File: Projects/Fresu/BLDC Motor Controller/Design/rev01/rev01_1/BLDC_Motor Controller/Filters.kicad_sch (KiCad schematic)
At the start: 0 parts

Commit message: UPDATE 9
COMPLETED FILTERS SCHEMATIC
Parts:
- added C44, C50, C52, C54: 100n, symbol Device:C
- added C48, C49, C51, C53: 4n7, symbol Device:C
- added J8: Conn_01x06, symbol Connector_Generic:Conn_01x06
- added R38, R44, R46: 2k2, symbol Device:R
- added R43, R45, R47, R48: 10k, symbol Device:R
- added R49: 0R, symbol Device:R
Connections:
- new net +3V3: C44.1, C50.1, C52.1, C54.1, R38.1, R44.1, R46.1, R48.1
- new net +5V: J8.1 (Pin_1)
- new net GND: C44.2, C48.2, C49.2, C50.2, C51.2, C52.2, C53.2, C54.2, J8.6 (Pin_6)
- new net HALL_1_IN: C48.1, J8.3 (Pin_3), R38.2, R43.1
- new net HALL_1_OUT: R43.2
- new net HALL_2_IN: C49.1, J8.4 (Pin_4), R44.2, R45.1
- new net HALL_2_OUT: R45.2
- new net HALL_3_IN: C51.1, J8.5 (Pin_5), R46.2, R47.1
- new net HALL_3_OUT: R47.2
- new net TEMP_IN: C53.1, J8.2 (Pin_2), R48.2, R49.1
- new net TEMP_MOTOR: R49.2
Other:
- note added: "HALL ENCODER TO MCU =>"
- note added: "HALL_1 FILTER"
- note added: "HALL_2 FILTER"
- note added: "HALL_3 FILTER"
- note added: "OUTPUT"
- note added: "TEMP_MOTOR FILTER"

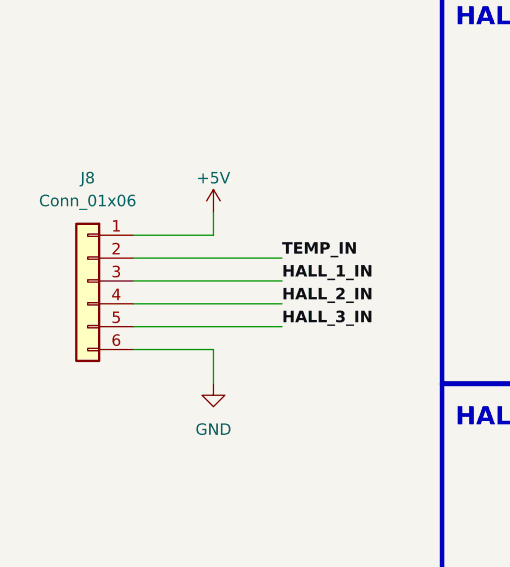
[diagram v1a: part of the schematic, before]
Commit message: Update 13
Added:
1) USB Schematic
2) footprints to all parts
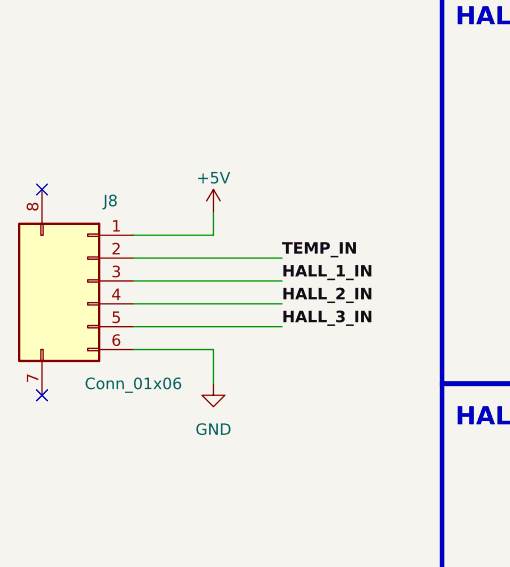
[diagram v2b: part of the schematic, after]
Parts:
- C44, C48, C49, C50, C51, C52, C53, C54: footprint (none) -> Capacitor_SMD:C_0603_1608Metric
- J8: footprint (none) -> DF_ESC_Footprint_Library:CONN-SMD_S6B-XH-SM4-TB-LF-SN
- R38, R43, R44, R45, R46, R47, R48, R49: footprint (none) -> Resistor_SMD:R_0603_1608Metric_Pad0.98x0.95mm_HandSolder
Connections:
- no-connect marks 0 -> 2
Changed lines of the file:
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@@
   (junction (at 93.98 41.91) (diameter 0) (color 0 0 0 0)
   )
+  (no_connect (at 22.86 104.14))
+  (no_connect (at 22.86 81.28))
   (polyline (pts (xy 128.27 58.42) (xy 67.31 58.42))
     (stroke (width 0.5) (type default))
@@
       (effects (font (size 1.27 1.27)) (justify left))
     )
-    (property "Footprint" "" (at 92.202 76.2 90)
+    (property "Footprint" "Resistor_SMD:R_0603_1608Metric_Pad0.98x0.95mm_HandSolder" (at 92.202 76.2 90)
       (effects (font (size 1.27 1.27)) hide)
     )
@@
       (effects (font (size 1.27 1.27)) (justify left))
     )
-    (property "Footprint" "" (at 110.1852 121.92 0)
+    (property "Footprint" "Capacitor_SMD:C_0603_1608Metric" (at 110.1852 121.92 0)
       (effects (font (size 1.27 1.27)) hide)
     )
@@
       (effects (font (size 1.27 1.27)) (justify left))
     )
-    (property "Footprint" "" (at 110.1852 33.02 0)
+    (property "Footprint" "Capacitor_SMD:C_0603_1608Metric" (at 110.1852 33.02 0)
       (effects (font (size 1.27 1.27)) hide)
     )
@@
       (effects (font (size 1.27 1.27)) (justify left))
     )
-    (property "Footprint" "" (at 110.1852 77.47 0)
+    (property "Footprint" "Capacitor_SMD:C_0603_1608Metric" (at 110.1852 77.47 0)
       (effects (font (size 1.27 1.27)) hide)
     )
@@
       (effects (font (size 1.27 1.27)) (justify left))
     )
-    (property "Footprint" "" (at 94.9452 52.07 0)
+    (property "Footprint" "Capacitor_SMD:C_0603_1608Metric" (at 94.9452 52.07 0)
       (effects (font (size 1.27 1.27)) hide)
     )
@@
       (effects (font (size 1.27 1.27)))
     )
-    (property "Footprint" "" (at 102.87 177.038 90)
+    (property "Footprint" "Resistor_SMD:R_0603_1608Metric_Pad0.98x0.95mm_HandSolder" (at 102.87 177.038 90)
       (effects (font (size 1.27 1.27)) hide)
     )
@@
       (effects (font (size 1.27 1.27)))
     )
-    (property "Footprint" "" (at 102.87 88.138 90)
+    (property "Footprint" "Resistor_SMD:R_0603_1608Metric_Pad0.98x0.95mm_HandSolder" (at 102.87 88.138 90)
       (effects (font (size 1.27 1.27)) hide)
     )
@@
       (effects (font (size 1.27 1.27)) (justify left))
     )
-    (property "Footprint" "" (at 92.202 120.65 90)
+    (property "Footprint" "Resistor_SMD:R_0603_1608Metric_Pad0.98x0.95mm_HandSolder" (at 92.202 120.65 90)
       (effects (font (size 1.27 1.27)) hide)
     )
@@
       (effects (font (size 1.27 1.27)) (justify left))
     )
-    (property "Footprint" "" (at 110.1852 166.37 0)
+    (property "Footprint" "Capacitor_SMD:C_0603_1608Metric" (at 110.1852 166.37 0)
       (effects (font (size 1.27 1.27)) hide)
     )
@@
   (symbol (lib_id "Connector_Generic:Conn_01x06") (at 27.94 91.44 0) (mirror y) (unit 1)
     (in_bom yes) (on_board yes) (dnp no) (fields_autoplaced)
-    (property "Reference" "J8" (at 27.94 80.01 0)
-      (effects (font (size 1.27 1.27)))
-    )
-    (property "Value" "Conn_01x06" (at 27.94 82.55 0)
-      (effects (font (size 1.27 1.27)))
-    )
-    (property "Footprint" "" (at 27.94 91.44 0)
+    (property "Reference" "J8" (at 30.48 82.55 0)
+      (effects (font (size 1.27 1.27)))
+    )
+    (property "Value" "Conn_01x06" (at 33.02 102.87 0)
+      (effects (font (size 1.27 1.27)))
+    )
+    (property "Footprint" "DF_ESC_Footprint_Library:CONN-SMD_S6B-XH-SM4-TB-LF-SN" (at 27.94 91.44 0)
       (effects (font (size 1.27 1.27)) hide)
     )
@@
     (pin "1")
     (pin "2")
+    (pin "8")
+    (pin "7")
     (instances
       (project "BLDC_Motor Controller"
@@
       (effects (font (size 1.27 1.27)) (justify left))
     )
-    (property "Footprint" "" (at 92.202 165.1 90)
+    (property "Footprint" "Resistor_SMD:R_0603_1608Metric_Pad0.98x0.95mm_HandSolder" (at 92.202 165.1 90)
       (effects (font (size 1.27 1.27)) hide)
     )
@@
       (effects (font (size 1.27 1.27)) (justify left))
     )
-    (property "Footprint" "" (at 94.9452 140.97 0)
+    (property "Footprint" "Capacitor_SMD:C_0603_1608Metric" (at 94.9452 140.97 0)
       (effects (font (size 1.27 1.27)) hide)
     )
@@
       (effects (font (size 1.27 1.27)) (justify left))
     )
-    (property "Footprint" "" (at 92.202 31.75 90)
+    (property "Footprint" "Resistor_SMD:R_0603_1608Metric_Pad0.98x0.95mm_HandSolder" (at 92.202 31.75 90)
       (effects (font (size 1.27 1.27)) hide)
     )
@@
       (effects (font (size 1.27 1.27)))
     )
-    (property "Footprint" "" (at 102.87 132.588 90)
+    (property "Footprint" "Resistor_SMD:R_0603_1608Metric_Pad0.98x0.95mm_HandSolder" (at 102.87 132.588 90)
       (effects (font (size 1.27 1.27)) hide)
     )
@@
       (effects (font (size 1.27 1.27)) (justify left))
     )
-    (property "Footprint" "" (at 94.9452 185.42 0)
+    (property "Footprint" "Capacitor_SMD:C_0603_1608Metric" (at 94.9452 185.42 0)
       (effects (font (size 1.27 1.27)) hide)
     )
@@
       (effects (font (size 1.27 1.27)) (justify left))
     )
-    (property "Footprint" "" (at 94.9452 96.52 0)
+    (property "Footprint" "Capacitor_SMD:C_0603_1608Metric" (at 94.9452 96.52 0)
       (effects (font (size 1.27 1.27)) hide)
     )
@@
       (effects (font (size 1.27 1.27)))
     )
-    (property "Footprint" "" (at 102.87 43.688 90)
-      (effects (font (size 1.27 1.27)) hide)
-    )
+    (property "Footprint" "Resistor_SMD:R_0603_1608Metric_Pad0.98x0.95mm_HandSolder" (at 102.87 43.688 90)
+      (effects (font (size 1.27 1.27)) hide)
+    )

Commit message: Update 15
Fixing some schematic errors

initial layout of larger component complete
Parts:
- removed J8: Conn_01x06, DF_ESC_Footprint_Library:CONN-SMD_S6B-XH-SM4-TB-LF-SN, symbol Connector_Generic:Conn_01x06
- added J7: Conn_01x06, DF_ESC_Footprint_Library:CONN-SMD_S6B-XH-SM4-TB-LF-SN, symbol Connector_Generic:Conn_01x06
- renumbered C48 to C47, C49 to C48, C51 to C49, C53 to C50, C44 to C51, C50 to C52, C52 to C53, R38 to R43, R46 to R45, R48 to R46, R43 to R47, R45 to R48, R47 to R49, R49 to R50
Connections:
- net +5V: now also J7.6 (Pin_6)
- net GND: now also J7.1 (Pin_1)
- net HALL_1_IN: now also J7.4 (Pin_4)
- net HALL_2_IN: now also J7.3 (Pin_3)
- net HALL_3_IN: now also J7.2 (Pin_2)
- net TEMP_IN: now also J7.5 (Pin_5)

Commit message: Update 26
Matched DF's Designators to mine so I can use BOM as is

Updated MFR'ing files

Rev1 Ready for release
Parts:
- renumbered C47 to C50, C48 to C51, C49 to C52, C50 to C53, C51 to C54, C52 to C55, C53 to C56, C54 to C57, J7 to J9, R50 to R61
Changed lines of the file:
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@@
 		(on_board yes)
 		(dnp no)
-		(property "Reference" "C53"
+		(property "Reference" "C56"
 			(at 102.87 115.57 0)
 			(effects
@@
 			(project "BLDC_Motor Controller"
 				(path "/e63e39d7-6ac0-4ffd-8aa3-1841a4541b55/cf649508-ceea-40bc-abe4-7aa1a01e8c7e"
-					(reference "C53")
+					(reference "C56")
 					(unit 1)
 				)
@@
 		(on_board yes)
 		(dnp no)
-		(property "Reference" "C51"
+		(property "Reference" "C54"
 			(at 102.87 26.67 0)
 			(effects
@@
 			(project "BLDC_Motor Controller"
 				(path "/e63e39d7-6ac0-4ffd-8aa3-1841a4541b55/cf649508-ceea-40bc-abe4-7aa1a01e8c7e"
-					(reference "C51")
+					(reference "C54")
 					(unit 1)
 				)
@@
 		(on_board yes)
 		(dnp no)
-		(property "Reference" "J7"
+		(property "Reference" "J9"
 			(at 30.48 102.87 0)
 			(effects
@@
 			(project "BLDC_Motor Controller"
 				(path "/e63e39d7-6ac0-4ffd-8aa3-1841a4541b55/cf649508-ceea-40bc-abe4-7aa1a01e8c7e"
-					(reference "J7")
+					(reference "J9")
 					(unit 1)
 				)
@@
 		(on_board yes)
 		(dnp no)
-		(property "Reference" "C52"
+		(property "Reference" "C55"
 			(at 102.87 71.12 0)
 			(effects
@@
 			(project "BLDC_Motor Controller"
 				(path "/e63e39d7-6ac0-4ffd-8aa3-1841a4541b55/cf649508-ceea-40bc-abe4-7aa1a01e8c7e"
-					(reference "C52")
+					(reference "C55")
 					(unit 1)
 				)
@@
 		(on_board yes)
 		(dnp no)
-		(property "Reference" "C47"
+		(property "Reference" "C50"
 			(at 87.63 45.72 0)
 			(effects
@@
 			(project "BLDC_Motor Controller"
 				(path "/e63e39d7-6ac0-4ffd-8aa3-1841a4541b55/cf649508-ceea-40bc-abe4-7aa1a01e8c7e"
-					(reference "C47")
+					(reference "C50")
 					(unit 1)
 				)
@@
 		(on_board yes)
 		(dnp no)
-		(property "Reference" "R50"
+		(property "Reference" "R61"
 			(at 102.87 177.8 90)
 			(effects
@@
 			(project "BLDC_Motor Controller"
 				(path "/e63e39d7-6ac0-4ffd-8aa3-1841a4541b55/cf649508-ceea-40bc-abe4-7aa1a01e8c7e"
-					(reference "R50")
+					(reference "R61")
 					(unit 1)
 				)
@@
 		(on_board yes)
 		(dnp no)
-		(property "Reference" "C54"
+		(property "Reference" "C57"
 			(at 102.87 160.02 0)
 			(effects
@@
 			(project "BLDC_Motor Controller"
 				(path "/e63e39d7-6ac0-4ffd-8aa3-1841a4541b55/cf649508-ceea-40bc-abe4-7aa1a01e8c7e"
-					(reference "C54")
+					(reference "C57")
 					(unit 1)
 				)
@@
 		(on_board yes)
 		(dnp no)
-		(property "Reference" "C49"
+		(property "Reference" "C52"
 			(at 87.63 134.62 0)
 			(effects
@@
 			(project "BLDC_Motor Controller"
 				(path "/e63e39d7-6ac0-4ffd-8aa3-1841a4541b55/cf649508-ceea-40bc-abe4-7aa1a01e8c7e"
-					(reference "C49")
+					(reference "C52")
 					(unit 1)
 				)
@@
 		(on_board yes)
 		(dnp no)
-		(property "Reference" "C50"
+		(property "Reference" "C53"
 			(at 87.63 179.07 0)
 			(effects
@@
 			(project "BLDC_Motor Controller"
 				(path "/e63e39d7-6ac0-4ffd-8aa3-1841a4541b55/cf649508-ceea-40bc-abe4-7aa1a01e8c7e"
-					(reference "C50")
+					(reference "C53")
 					(unit 1)
 				)
@@
 		(on_board yes)
 		(dnp no)
-		(property "Reference" "C48"
+		(property "Reference" "C51"
 			(at 87.63 90.17 0)
 			(effects
@@
 			(project "BLDC_Motor Controller"
 				(path "/e63e39d7-6ac0-4ffd-8aa3-1841a4541b55/cf649508-ceea-40bc-abe4-7aa1a01e8c7e"
-					(reference "C48")
-					(unit 1)
-				)
+					(reference "C51")
+					(unit 1)
+				)
